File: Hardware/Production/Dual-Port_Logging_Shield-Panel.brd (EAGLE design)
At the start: 137.4 x 177.3 mm, 1686 parts, among them IC1 USB224X_2241_V04, IC10 USB224X_2241_V04, IC11 USB224X_2241_V04, IC12 USB224X_2241_V04, IC13 USB224X_2241_V04, IC14 USB224X_2241_V04, IC2 USB224X_2241_V04, IC3 USB224X_2241_V04, IC4 USB224X_2241_V04, IC5 USB224X_2241_V04, IC6 USB224X_2241_V04, IC7 USB224X_2241_V04, IC8 USB224X_2241_V04, IC9 USB224X_2241_V04, J10 MICRO-SD-PUSH-PUSH-EXT-PIN, J11 AVR_SPI_PROG_3X2TESTPOINTS, J12 THING_PLUS, J14 MICRO-SD-PUSH-PUSH-EXT-PIN, J15 AVR_SPI_PROG_3X2TESTPOINTS, J16 THING_PLUS, J18 MICRO-SD-PUSH-PUSH-EXT-PIN, J19 AVR_SPI_PROG_3X2TESTPOINTS, J2 MICRO-SD-PUSH-PUSH-EXT-PIN, J20 THING_PLUS, J22 MICRO-SD-PUSH-PUSH-EXT-PIN, J23 AVR_SPI_PROG_3X2TESTPOINTS, J24 THING_PLUS, J26 MICRO-SD-PUSH-PUSH-EXT-PIN, J27 AVR_SPI_PROG_3X2TESTPOINTS, J28 THING_PLUS, J3 AVR_SPI_PROG_3X2TESTPOINTS, J30 MICRO-SD-PUSH-PUSH-EXT-PIN, J31 AVR_SPI_PROG_3X2TESTPOINTS, J32 THING_PLUS, J34 MICRO-SD-PUSH-PUSH-EXT-PIN, J35 AVR_SPI_PROG_3X2TESTPOINTS, J36 THING_PLUS, J38 MICRO-SD-PUSH-PUSH-EXT-PIN, J39 AVR_SPI_PROG_3X2TESTPOINTS, J4 THING_PLUS, J40 THING_PLUS, J42 MICRO-SD-PUSH-PUSH-EXT-PIN, J43 AVR_SPI_PROG_3X2TESTPOINTS, J44 THING_PLUS, J46 MICRO-SD-PUSH-PUSH-EXT-PIN, J47 AVR_SPI_PROG_3X2TESTPOINTS, J48 THING_PLUS, J50 MICRO-SD-PUSH-PUSH-EXT-PIN, J51 AVR_SPI_PROG_3X2TESTPOINTS, J52 THING_PLUS, J54 MICRO-SD-PUSH-PUSH-EXT-PIN, J55 AVR_SPI_PROG_3X2TESTPOINTS, J56 THING_PLUS, J6 MICRO-SD-PUSH-PUSH-EXT-PIN, J7 AVR_SPI_PROG_3X2TESTPOINTS, J8 THING_PLUS, Q1 20V/4.2A/52mΩ/1.4W, Q10 20V/0.2A/8MHz/1.2Ω/1Vth, Q11 20V/4.2A/52mΩ/1.4W, Q13 20V/4.2A/52mΩ/1.4W, Q15 20V/4.2A/52mΩ/1.4W, Q16 20V/4.2A/52mΩ/1.4W, Q17 20V/0.2A/8MHz/1.2Ω/1Vth, Q18 20V/4.2A/52mΩ/1.4W, Q2 20V/0.2A/8MHz/1.2Ω/1Vth, Q20 20V/4.2A/52mΩ/1.4W, Q22 20V/4.2A/52mΩ/1.4W, Q23 20V/4.2A/52mΩ/1.4W, Q24 20V/0.2A/8MHz/1.2Ω/1Vth, Q25 20V/4.2A/52mΩ/1.4W, Q27 20V/4.2A/52mΩ/1.4W, Q29 20V/4.2A/52mΩ/1.4W, Q3 20V/4.2A/52mΩ/1.4W, Q30 20V/4.2A/52mΩ/1.4W, Q31 20V/0.2A/8MHz/1.2Ω/1Vth, Q32 20V/4.2A/52mΩ/1.4W, Q34 20V/4.2A/52mΩ/1.4W, Q36 20V/4.2A/52mΩ/1.4W, Q37 20V/4.2A/52mΩ/1.4W, Q38 20V/0.2A/8MHz/1.2Ω/1Vth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

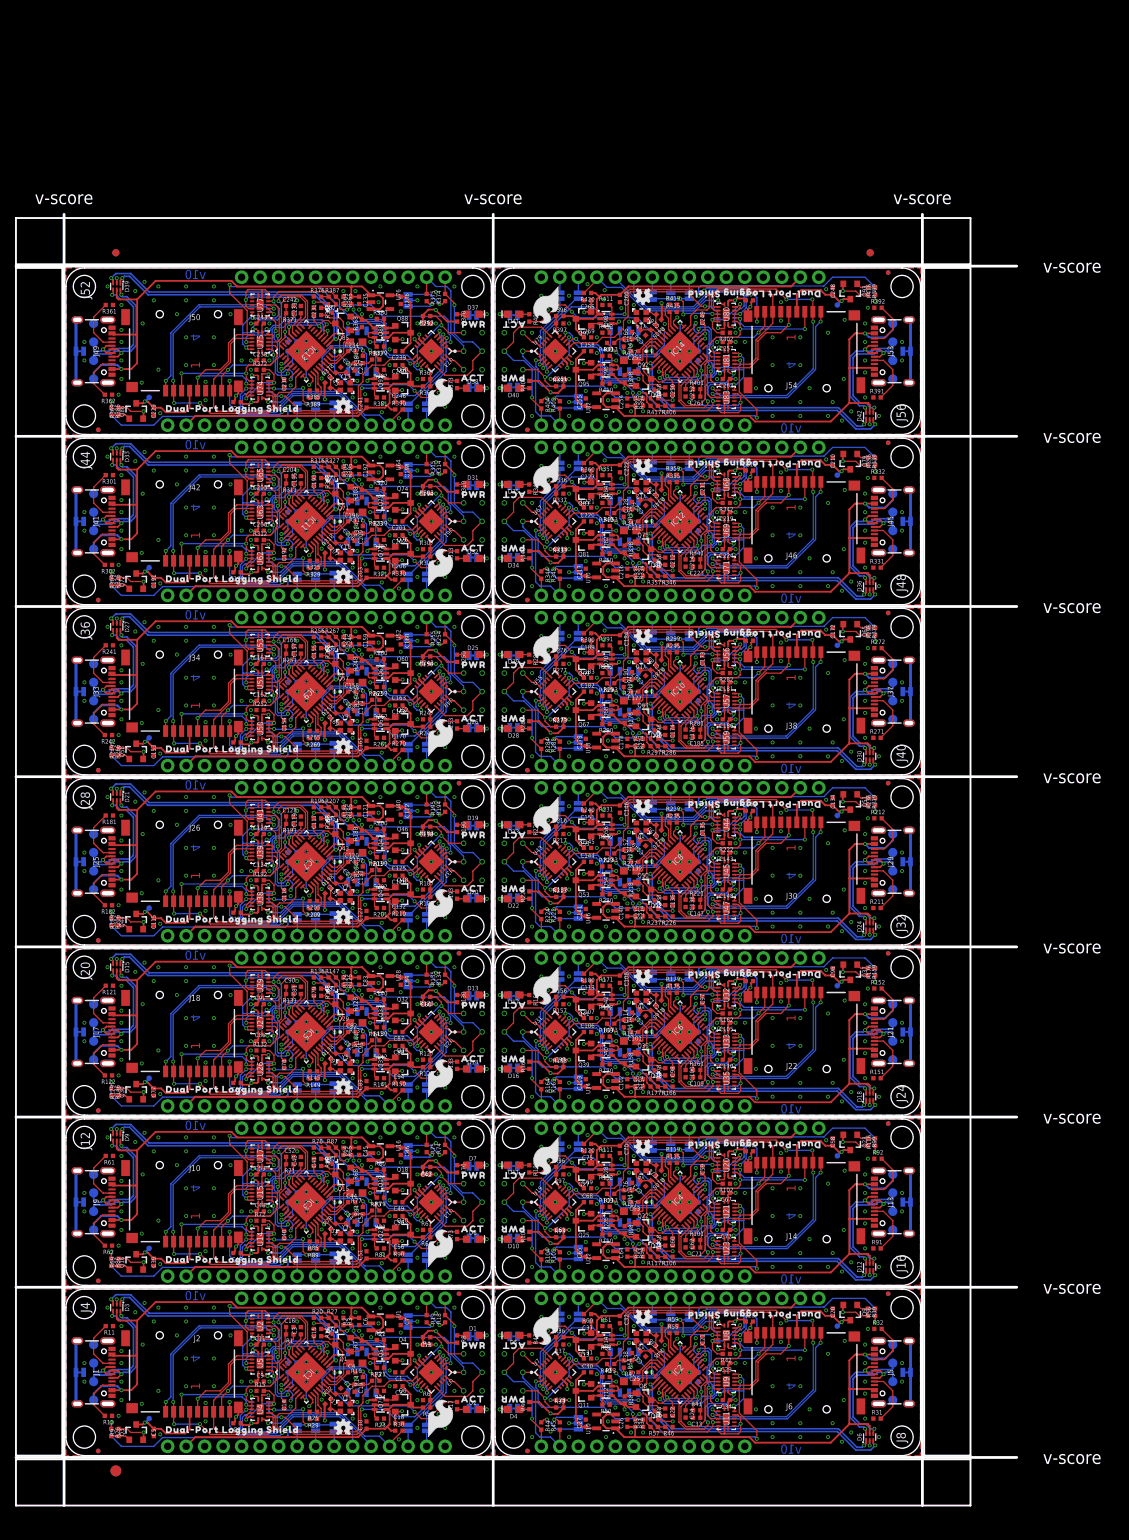
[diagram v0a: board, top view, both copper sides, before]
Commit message: Updated hardware files after REDS Review
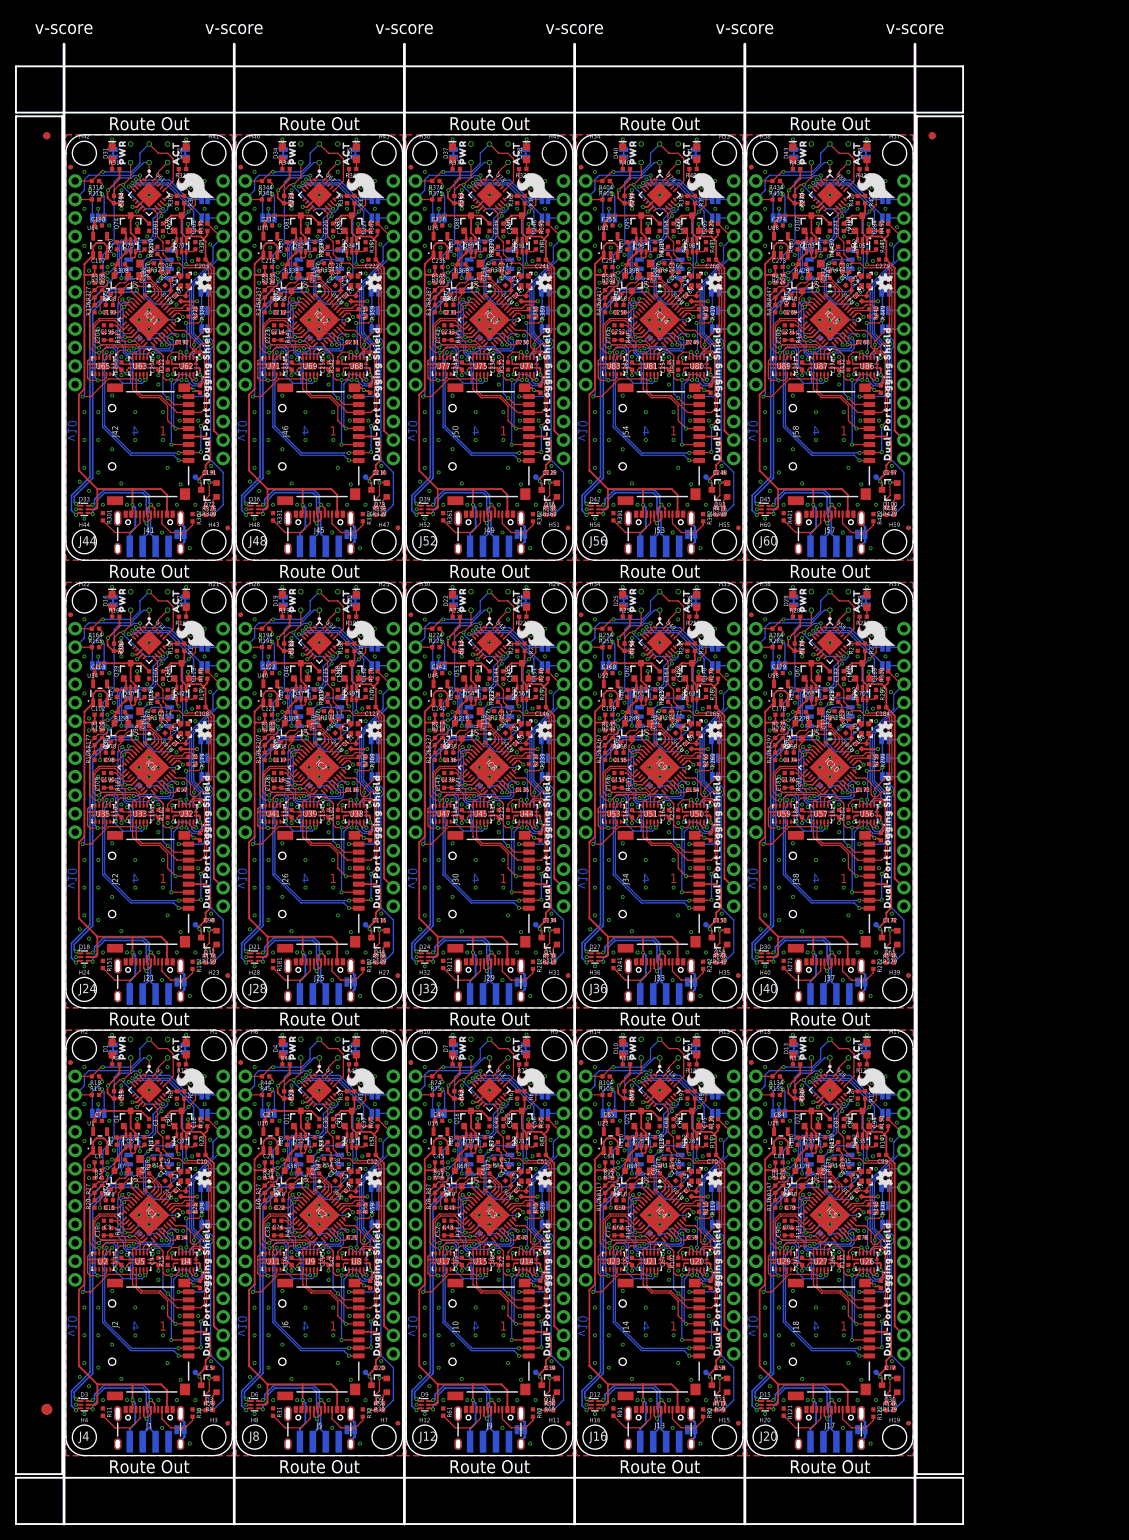
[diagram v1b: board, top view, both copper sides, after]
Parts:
- removed D+, D+1, D+10, D+11, D+12, D+13, D+2, D+3, D+4, D+5, D+6, D+7, D+8, D+9, D-, D-1, D-10, D-11, D-12, D-13, D-2, D-3, D-4, D-5, D-6, D-7, D-8, D-9, GND, GND1, GND10, GND11, GND12, GND13, GND2, GND3, GND4, GND5, GND6, GND7, GND8, GND9, V_USB, V_USB1, V_USB10, V_USB11, V_USB12, V_USB13, V_USB2, V_USB3, V_USB4, V_USB5, V_USB6, V_USB7, V_USB8, V_USB9: TEST-POINT3X5, SparkFun-Connectors:PAD.03X.05
- added C267, C268, C270, C275, C276, C277, C278, C280, C281, C285: 0.1uF, SparkFun-Capacitors:0402-TIGHT
- added C269, C271, C272, C273, C274, C279, C284: 2.2uF, SparkFun-Capacitors:0402-TIGHT
- added C282, C283: 12pF, SparkFun-Capacitors:0402-TIGHT
- added D43: RED, SparkFun-LED:LED-0603
- added D44: Yellow, SparkFun-LED:LED-0603
- added D45: PRTR5V0U2F, SparkFun-IC-Power:SOT886
- added FD57, FD58, FD59, FD60: FIDUCIALUFIDUCIAL, SparkFun-Aesthetics:FIDUCIAL-MICRO
- added GPIO15, MICROSD_VCC14, SDIO_!RESET!14, SDIO_VDD14: TEST-POINT3, SparkFun-Connectors:PAD.03X.03
- added H1, H10, H11, H12, H13, H14, H15, H16, H17, H18, H19, H2, H20, H21, H22, H23, H24, H25, H26, H27, H28, H29, H3, H30, H31, H32, H33, H34, H35, H36, H37, H38, H39, H4, H40, H41, H42, H43, H44, H45, H46, H47, H48, H49, H5, H50, H51, H52, H53, H54, H55, H56, H57, H58, H59, H6, H60, H7, H8, H9: STAND-OFF, SparkFun-Hardware:STAND-OFF
- added I2C14: JUMPER-SMT_3_NO_SILK, SparkFun-Jumpers:SMT-JUMPER_3_NO_SILK
- added IC15: USB224X_2241_V04, SparkFun-IC-Special-Function:36-QFN
- added J57: (no value), SparkFun-Connectors:USB-C-16P_4LAYER-PADS
- added J58: MICRO-SD-PUSH-PUSH-EXT-PIN, SparkFun-Connectors:MICROSD-EXTERNALPIN
- added J59: AVR_SPI_PROG_3X2TESTPOINTS, SparkFun-Connectors:2X3_TEST_POINTS
- added J60: THING_PLUS, SparkFun-Boards:THING_PLUS
- added JP43, JP46, JP47, JP50, JP51, JP54, JP55, JP58, JP59, RXD14, TXD14: JUMPER-SMT_2_NO_SILK, SparkFun-Jumpers:SMT-JUMPER_2_NO_SILK
- added JP44, JP48, JP52, JP56, JP60: USB_SOLDER_PADS, SparkFun-Connectors:USB-SOLDER-PADS
- added JP45, JP49, JP53, JP57, LED29, LED30: JUMPER-SMT_2_NC_TRACE_SILK, SparkFun-Jumpers:SMT-JUMPER_2_NC_TRACE_SILK
- added LOGO57, LOGO58: OSHW-LOGOMINI, SparkFun-Aesthetics:OSHW-LOGO-MINI
- added LOGO59: SFE_LOGO_FLAME.2_INCH, SparkFun-Aesthetics:SFE_LOGO_FLAME_.2
- added LOGO60: SFE_LOGO_NAME_FLAME.1_INCH, SparkFun-Aesthetics:SFE_LOGO_NAME_FLAME_.1
- added Q100, Q102, Q104, Q99: 20V/4.2A/52mΩ/1.4W, SparkFun-DiscreteSemi:SOT23-3
- added Q101: 20V/0.2A/8MHz/1.2Ω/1Vth, SparkFun-DiscreteSemi:SOT-416FL
- added Q103, Q105: (no value), SparkFun-DiscreteSemi:SOT363_PHILIPS
- added R421, R422: 5.1k, SparkFun-Resistors:0402-TIGHT
- added R423, R424, R425, R443, R444, R445, R449, R450: 10k, SparkFun-Resistors:0402-TIGHT
- added R426, R427, R428, R429, R431, R432, R436, R439, R441: 100k, SparkFun-Resistors:0402-TIGHT
- added R430, R433: 1k, SparkFun-Resistors:0402-TIGHT
- added R434, R435: 2.2k, SparkFun-Resistors:0402-TIGHT
- added R437: 12k, SparkFun-Resistors:0603
- added R438, R440, R442: 1M, SparkFun-Resistors:0402-TIGHT
- added R446, R447, R448: 100, SparkFun-Resistors:0402-TIGHT
- added SH14: JUMPER-SMT_2_NC_TRACE_NO-SILK, SparkFun-Jumpers:SMT-JUMPER_2_NC_TRACE_NO-SILK
- added U$337: (no value), output:PWR0
- added U$338: (no value), output:ACT0
- added U$339: (no value), output:#I�C#0
- added U$340: (no value), output:#PWR#0
- added U$341: (no value), output:#ACT#0
- added U$342, U$343: (no value), output:DUAL#PORT_LOGGING_SHIELD0
- added U$344: (no value), output:#SDA#0
- added U$345: (no value), output:#SCL#1
- added U$346: (no value), output:#RXD#0
- added U$347: (no value), output:#TXD#1
- added U$348: (no value), output:#POCI#0
- added U$349: (no value), output:#PICO#1
- added U$350: (no value), output:#SCK#2
- added U$351: (no value), output:#A5__#CS##0
- added U$352: (no value), output:#A4__#CS##6
- added U$353: (no value), output:#A3__#CS##6
- added U$354: (no value), output:#GND#0
- added U$355: (no value), output:#3V3#1
- added U$356: (no value), output:G0
- added U$357: (no value), output:V0
- added U$358: (no value), output:D#0
- added U$359: (no value), output:D#1
- added U$360: (no value), output:SH0
- added U85: ATTINY841-ARDUINO_QFN20M1, SparkFun-IC-Microcontroller:QFN20_20M1
- added U86, U87, U89: 74HC4066_QUAD_BILATERAL_SWITCH_QFN, SparkFun-IC-Logic:14-QFN
- added U88: 3.3V, SparkFun-IC-Power:SOT23-5
- added U90: 24C04, SparkFun-IC-Memory:SO08
- added Y15: 24MHz, SparkFun-Clocks:CRYSTAL-SMD-2.0X1.6MM
- J12, J16, J20, J24, J28, J32, J36, J4, J40, J44, J48, J52, J56, J8: device Thing_Plus:THING_PLUS -> SparkFun-Boards:THING_PLUS
- JP10, JP19, JP22, JP31, JP34, JP7: value JUMPER-SMT_2_NC_TRACE_SILK -> JUMPER-SMT_2_NO_SILK; device SparkFun-Jumpers:SMT-JUMPER_2_NC_TRACE_SILK -> SparkFun-Jumpers:SMT-JUMPER_2_NO_SILK
- JP12, JP20, JP24, JP32, JP36, JP8: value JUMPER-SMT_2_NO_SILK -> USB_SOLDER_PADS; device SparkFun-Jumpers:SMT-JUMPER_2_NO_SILK -> SparkFun-Connectors:USB-SOLDER-PADS
- JP16, JP28, JP4, JP40: value JUMPER-SMT_2_NC_TRACE_SILK -> USB_SOLDER_PADS; device SparkFun-Jumpers:SMT-JUMPER_2_NC_TRACE_SILK -> SparkFun-Connectors:USB-SOLDER-PADS
- JP17, JP21, JP29, JP33, JP41, JP5, JP9: value JUMPER-SMT_2_NO_SILK -> JUMPER-SMT_2_NC_TRACE_SILK; device SparkFun-Jumpers:SMT-JUMPER_2_NO_SILK -> SparkFun-Jumpers:SMT-JUMPER_2_NC_TRACE_SILK
- SH, SH1, SH10, SH11, SH12, SH13, SH2, SH3, SH4, SH5, SH6, SH7, SH8, SH9: value JUMPER-SMT_2_NC_TRACE_SILK -> JUMPER-SMT_2_NC_TRACE_NO-SILK; device SparkFun-Jumpers:SMT-JUMPER_2_NC_TRACE_SILK -> SparkFun-Jumpers:SMT-JUMPER_2_NC_TRACE_NO-SILK
- U$120, U$144, U$168, U$192, U$20, U$216, U$240, U$264, U$288, U$312, U$336, U$48, U$72, U$96: device output:#SH#0 -> output:SH0
- moved U$120 122.9 mm to (110.7, 3.56)
- moved SH4 120.4 mm to (109.2, 3.56), turned to 0 degrees
- moved U$116 119.4 mm to (107.6, 4.19)
- moved FD18 119.2 mm to (115.7, 4.45), turned to 0 degrees
- moved FD19 119.2 mm to (115.7, 4.45), turned to 0 degrees
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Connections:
- new net !CS!14: JP57.2, JP58.2, JP59.2, U86.4
- new net !RESET!14: J59.5, R423.1, U85.13
- new net 3.3V14: C278.1, C279.1, J60.27, Q104.3, Q105.1, R426.2, R450.1
- new net 3V3_DIV_15: R426.1, R427.2, U85.15
- new net ACTIVITY14: IC15.1, R433.2
- new net AT_POCI14: J59.1, U85.20
- new net D+14: D45.1, IC15.2
- new net D+_IN14: D45.6, J57.A6, J57.B6, JP60.D+
- new net D-14: D45.3, IC15.3
- new net D-_IN14: D45.4, J57.A7, J57.B7, JP60.D-
- new net GND14: C267.2, C268.2, C269.2, C270.2, C271.2, C272.2, C273.2, C274.2, C275.2, C276.2, C277.2, C278.2, C279.2, C280.2, C281.2, C282.1, C283.1, C284.2, C285.2, D45.2, IC15.28, IC15.EPAD, J57.GND, J57.GND2, J58.10, J58.11, J58.12, J58.13, J58.6, J59.6, J60.25, JP60.GND, LED29.1, LED30.1, Q101.2, R421.1, R422.1, R425.1, R427.1, R432.1, R436.1, R437.1, R439.1, R440.1, R441.1, R442.1, R445.2, R449.2, SH14.2, U85.8, U85.PAD, U86.7, U86.EPAD, U87.7, U87.EPAD, U88.2, U89.12, U89.6, U89.7, U89.EPAD, U90.1, U90.2, U90.3, U90.4, U90.7
- new net GPIO57: IC15.27, R443.2, U90.5
- new net GPIO58: IC15.29, R445.1
- new net GPIO59: IC15.31, R444.2, U90.6
- new net GPIO60: GPIO15.1, IC15.21
- new net MICROSD_CLK/SCK14: J58.5, U85.12, U86.10, U87.9
- new net MICROSD_CMD/SDI14: J58.3, U86.9, U87.3
- new net MICROSD_D0/SDO14: J58.7, U86.2, U87.10
- new net MICROSD_D29: J58.1, U89.3
- new net MICROSD_D3/!CS!14: J58.2, U86.3, U89.2
- new net MICROSD_D30: J58.8, U87.2
- new net MICROSD_PWR_EN14: R446.1, U85.5
- new net MICROSD_VCC14: C267.1, J58.4, MICROSD_VCC14.1, Q100.3
- new net N$365: J57.A5, R421.2
- new net N$366: J57.B5, R422.2
- new net N$367: J60.19, JP57.1
- new net N$368: J60.20, JP58.1
- new net N$369: J60.21, JP59.1
- new net N$370: D43.A, R430.1
- new net N$371: D43.C, LED29.2
- new net N$372: D44.A, R433.1
- new net N$373: D44.C, LED30.2
- new net N$374: I2C14.3, R435.2
- new net N$375: I2C14.1, R434.1
- new net N$376: C271.1, IC15.13
- new net N$377: C272.1, IC15.34
- new net N$378: Q99.1, R428.1, R448.2
- new net N$379: IC15.35, R437.2
- new net N$380: J60.14, RXD14.1
- new net N$381: J60.15, TXD14.1
- new net N$382: Q103.2, Q103.5, Q103.6, R439.2
- new net N$383: Q102.1, Q103.3, R440.2
- new net N$384: Q105.2, Q105.5, Q105.6, R441.2
- new net N$385: Q104.1, Q105.3, R442.2
- new net N$386: Q100.1, R429.1, R446.2
- new net N$387: Q101.1, R436.2, R447.1
- new net N$388: Q101.3, R448.1
- new net N$389: J57.SHLD1, J57.SHLD2, J57.SHLD3, J57.SHLD4, SH14.1
- new net N$390: IC15.30, R449.1
- new net PICO14: J60.17, U86.8
- new net POCI14: J60.16, R450.2, U86.1
- new net RXD14: RXD14.2, U85.3
- new net SCL14: J59.3, J60.2, R435.1, U85.1
- new net SCLK14: J60.18, U86.11
- new net SDA14: J59.4, J60.1, R434.2, U85.16
- new net SDIO_!RESET!14: C280.1, IC15.18, R431.2, SDIO_!RESET!14.1
- new net SDIO_EN14: R447.2, U85.2, U87.12, U87.13, U87.5, U87.6, U89.13, U89.5
- new net SDIO_VDD14: C268.1, C269.1, C285.1, IC15.14, IC15.22, IC15.36, IC15.6, Q99.3, R431.1, R443.1, R444.1, SDIO_VDD14.1, U90.8
- new net SD_!CD!14: IC15.26, J58.9
- new net SD_CLK14: IC15.9, U87.8
- new net SD_CMD14: IC15.11, U87.4
- new net SD_D56: IC15.5, U87.11
- new net SD_D57: IC15.4, U87.1
- new net SD_D58: IC15.25, U89.4
- new net SD_D59: IC15.23, U89.1
- new net SPI_EN14: R432.2, U85.11, U86.12, U86.13, U86.5, U86.6
- new net TXD14: TXD14.2, U85.4
- new net VCC14: C270.1, C275.1, C276.1, C281.1, C284.1, I2C14.2, J59.2, Q100.2, Q102.2, Q103.4, Q104.2, Q105.4, Q99.2, R423.2, R428.2, R429.2, R430.2, U85.9, U86.14, U87.14, U89.14
- new net VCC_15: C274.1, C277.1, Q102.3, Q103.1, U88.5
- new net V_USB14: C273.1, D45.5, J57.VBUS1, J57.VBUS2, JP60.VBUS, R424.2, U88.1, U88.3
- new net V_USB_DIV_15: R424.1, R425.2, U85.14
- new net XTAL29: C283.2, IC15.32, R438.1, Y15.1
- new net XTAL30: C282.2, IC15.33, R438.2, Y15.3
- net !CS!1: now also JP7.2; no longer JP4.2
- net !CS!10: now also JP41.2, JP42.2, JP43.2; no longer JP31.2, JP32.2, JP33.2
- net !CS!11: now also JP45.2, JP46.2, JP47.2; no longer JP34.2, JP35.2, JP36.2
- net !CS!12: now also JP49.2, JP50.2, JP51.2; no longer JP37.2, JP38.2, JP39.2
- net !CS!13: now also JP53.2, JP54.2, JP55.2; no longer JP40.2, JP41.2, JP42.2
- net !CS!2: now also JP10.2, JP11.2; no longer JP7.2, JP8.2
- net !CS!3: now also JP13.2, JP14.2, JP15.2; no longer JP10.2, JP11.2, JP12.2
- net !CS!4: now also JP17.2, JP18.2, JP19.2; no longer JP13.2, JP14.2, JP15.2
- net !CS!5: now also JP21.2, JP22.2, JP23.2; no longer JP16.2, JP17.2, JP18.2
- net !CS!6: now also JP25.2, JP26.2, JP27.2; no longer JP19.2, JP20.2, JP21.2
- net !CS!7: now also JP29.2, JP30.2, JP31.2; no longer JP22.2, JP23.2, JP24.2
- net !CS!8: now also JP33.2, JP34.2, JP35.2; no longer JP25.2, JP26.2, JP27.2
- net !CS!9: now also JP37.2, JP38.2, JP39.2; no longer JP28.2, JP29.2, JP30.2
- net D+_IN: now also JP4.D+; no longer D+.1
- net D+_IN1: now also JP8.D+; no longer D+1.1
- net D+_IN10: now also JP44.D+; no longer D+10.1
- net D+_IN11: now also JP48.D+; no longer D+11.1
- net D+_IN12: now also JP52.D+; no longer D+12.1
- net D+_IN13: now also JP56.D+; no longer D+13.1
- net D+_IN2: now also JP12.D+; no longer D+2.1
- net D+_IN3: now also JP16.D+; no longer D+3.1
- net D+_IN4: now also JP20.D+; no longer D+4.1
- net D+_IN5: now also JP24.D+; no longer D+5.1
- net D+_IN6: now also JP28.D+; no longer D+6.1
- net D+_IN7: now also JP32.D+; no longer D+7.1
- net D+_IN8: now also JP36.D+; no longer D+8.1
- net D+_IN9: now also JP40.D+; no longer D+9.1
- net D-_IN: now also JP4.D-; no longer D-.1
- net D-_IN1: now also JP8.D-; no longer D-1.1
- net D-_IN10: now also JP44.D-; no longer D-10.1
- net D-_IN11: now also JP48.D-; no longer D-11.1
- net D-_IN12: now also JP52.D-; no longer D-12.1
- net D-_IN13: now also JP56.D-; no longer D-13.1
- net D-_IN2: now also JP12.D-; no longer D-2.1
- net D-_IN3: now also JP16.D-; no longer D-3.1
- net D-_IN4: now also JP20.D-; no longer D-4.1
- net D-_IN5: now also JP24.D-; no longer D-5.1
- net D-_IN6: now also JP28.D-; no longer D-6.1
- net D-_IN7: now also JP32.D-; no longer D-7.1
- net D-_IN8: now also JP36.D-; no longer D-8.1
- net D-_IN9: now also JP40.D-; no longer D-9.1
- net GND: now also JP4.GND; no longer GND.1
- net GND1: now also JP8.GND; no longer GND1.1
- net GND10: now also JP44.GND; no longer GND10.1
- net GND11: now also JP48.GND; no longer GND11.1
- net GND12: now also JP52.GND; no longer GND12.1
- net GND13: now also JP56.GND; no longer GND13.1
- net GND2: now also JP12.GND; no longer GND2.1
- net GND3: now also JP16.GND; no longer GND3.1
- net GND4: now also JP20.GND; no longer GND4.1
- net GND5: now also JP24.GND; no longer GND5.1
- net GND6: now also JP28.GND; no longer GND6.1
- net GND7: now also JP32.GND; no longer GND7.1
- net GND8: now also JP36.GND; no longer GND8.1
- net GND9: now also JP40.GND; no longer GND9.1
- net N$107: now also JP17.1; no longer JP13.1
- net N$108: now also JP18.1; no longer JP14.1
- net N$109: now also JP19.1; no longer JP15.1
- net N$133: now also JP21.1; no longer JP16.1
- net N$134: now also JP22.1; no longer JP17.1
- net N$135: now also JP23.1; no longer JP18.1
- net N$159: now also JP25.1; no longer JP19.1
- net N$160: now also JP26.1; no longer JP20.1
- net N$161: now also JP27.1; no longer JP21.1
- net N$185: now also JP29.1; no longer JP22.1
- net N$186: now also JP30.1; no longer JP23.1
- net N$187: now also JP31.1; no longer JP24.1
- net N$211: now also JP33.1; no longer JP25.1
- net N$212: now also JP34.1; no longer JP26.1
- net N$213: now also JP35.1; no longer JP27.1
- net N$237: now also JP37.1; no longer JP28.1
- net N$238: now also JP38.1; no longer JP29.1
- net N$239: now also JP39.1; no longer JP30.1
- net N$263: now also JP41.1; no longer JP31.1
- net N$264: now also JP42.1; no longer JP32.1
- net N$265: now also JP43.1; no longer JP33.1
- net N$289: now also JP45.1; no longer JP34.1
- net N$29: now also JP5.1; no longer JP4.1
- net N$290: now also JP46.1; no longer JP35.1
- net N$291: now also JP47.1; no longer JP36.1
- net N$30: now also JP6.1; no longer JP5.1
- net N$31: now also JP7.1; no longer JP6.1
- net N$315: now also JP49.1; no longer JP37.1
- net N$316: now also JP50.1; no longer JP38.1
- net N$317: now also JP51.1; no longer JP39.1
- net N$341: now also JP53.1; no longer JP40.1
- net N$342: now also JP54.1; no longer JP41.1
- net N$343: now also JP55.1; no longer JP42.1
- net N$55: now also JP9.1; no longer JP7.1
- net N$56: now also JP10.1; no longer JP8.1
- net N$57: now also JP11.1; no longer JP9.1
- net N$81: now also JP13.1; no longer JP10.1
- net N$82: now also JP14.1; no longer JP11.1
- net N$83: now also JP15.1; no longer JP12.1
- net V_USB: now also JP4.VBUS; no longer V_USB.1
- net V_USB1: now also JP8.VBUS; no longer V_USB1.1
- net V_USB10: now also JP44.VBUS; no longer V_USB10.1
- net V_USB11: now also JP48.VBUS; no longer V_USB11.1
- net V_USB12: now also JP52.VBUS; no longer V_USB12.1
- net V_USB13: now also JP56.VBUS; no longer V_USB13.1
- net V_USB2: now also JP12.VBUS; no longer V_USB2.1
- net V_USB3: now also JP16.VBUS; no longer V_USB3.1
- net V_USB4: now also JP20.VBUS; no longer V_USB4.1
- net V_USB5: now also JP24.VBUS; no longer V_USB5.1
- net V_USB6: now also JP28.VBUS; no longer V_USB6.1
- net V_USB7: now also JP32.VBUS; no longer V_USB7.1
- net V_USB8: now also JP36.VBUS; no longer V_USB8.1
- net V_USB9: now also JP40.VBUS; no longer V_USB9.1
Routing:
- net V_USB14: track 0.00 -> 67.5 mm, vias 0 -> 1
- net MICROSD_CLK/SCK14: track 0.00 -> 62.5 mm, vias 0 -> 4
- net MICROSD_PWR_EN14: track 0.00 -> 62.1 mm, vias 0 -> 4
- net SDIO_EN14: track 0.00 -> 52.2 mm, vias 0 -> 6
- net GND14: track 0.00 -> 46.6 mm, vias 0 -> 77
- net MICROSD_D3/!CS!14: track 0.00 -> 43.1 mm, vias 0 -> 4
- net 3.3V14: track 0.00 -> 41.4 mm
- net D-14: track 0.00 -> 39.5 mm, vias 0 -> 2
- net SPI_EN14: track 0.00 -> 39.0 mm, vias 0 -> 3
- net SDIO_VDD14: track 0.00 -> 38.0 mm, vias 0 -> 5
- net D+14: track 0.00 -> 37.1 mm, vias 0 -> 2
- net VCC14: track 0.00 -> 31.1 mm, vias 0 -> 12
- net PICO14: track 0.00 -> 26.1 mm, vias 0 -> 1
- net MICROSD_D29: track 0.00 -> 25.0 mm, vias 0 -> 2
- net POCI14: track 0.00 -> 23.2 mm, vias 0 -> 1
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- added copper zone on layer 1, net GND14
- added copper zone on layer 16, net GND14
- added copper zone on layer 2, net GND14
- added copper zone on layer 15, net VCC14
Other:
- board size 137.4 x 177.3 mm -> 130 x 203.2 mm
- board text added: "Route Out"

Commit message: PCB v1.1
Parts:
- added C286, C287, C288, C308, C309, C310, C311, C312, C332, C333, C334, C335, C336, C356, C357, C358, C359, C360: 10uF, SparkFun-Capacitors:0402-TIGHT
- added C289, C290, C292, C297, C298, C299, C300, C302, C303, C307, C313, C314, C316, C321, C322, C323, C324, C326, C327, C331, C337, C338, C340, C345, C346, C347, C348, C350, C351, C355: 0.1uF, SparkFun-Capacitors:0402-TIGHT
- added C291, C293, C294, C295, C296, C301, C306, C315, C317, C318, C319, C320, C325, C330, C339, C341, C342, C343, C344, C349, C354: 2.2uF, SparkFun-Capacitors:0402-TIGHT
- added C304, C305, C328, C329, C352, C353: 12pF, SparkFun-Capacitors:0402-TIGHT
- C100, C108, C121, C122, C132, C139, C146, C155, C158, C159, C170, C177, C178, C179, C193, C196, C203, C217, C227, C231, C235, C241, C25, C250, C252, C254, C255, C26, C265, C273, C274, C279, C43, C60, C62, C63, C81, C82, C83, C84, C98: value 2.2uF -> 0.1uF
- C104, C109, C114, C123, C125, C126, C128, C133, C147, C152, C162, C171, C173, C175, C181, C186, C199, C200, C205, C210, C219, C221, C223, C224, C229, C243, C247, C248, C258, C267, C270, C277, C29, C30, C31, C42, C53, C61, C66, C77, C78, C80, C85, C90, C99: value 0.1uF -> 2.2uF
- C111, C130, C131, C169, C187, C206, C207, C225, C226, C244, C283, C35, C36, C73, C74: value 12pF -> 0.1uF
- C113, C136, C160, C184, C208, C233, C41, C64, C65, C89: value 2.2uF -> 12pF
- C116, C118, C142, C143, C144, C164, C166, C167, C190, C191, C192, C20, C21, C213, C23, C237, C238, C239, C240, C261, C262, C285, C47, C48, C68, C69, C71, C72, C95, C96: value 0.1uF -> 10uF
- C117, C119, C120, C140, C141, C165, C189, C212, C214, C215, C216, C22, C236, C24, C260, C284, C44, C45, C46, C70, C94: value 2.2uF -> 10uF
- C137, C161, C185, C209, C232, C256, C257, C280, C281, C40, C88: value 0.1uF -> 12pF
- C149, C150, C245, C282, C54, C55: value 12pF -> 2.2uF
- C168, C188, C263, C264, C92, C93: value 12pF -> 10uF
- I2C, I2C1, I2C10, I2C11, I2C12, I2C13, I2C14, I2C2, I2C3, I2C4, I2C5, I2C6, I2C7, I2C8, I2C9: value JUMPER-SMT_3_NO_SILK -> JUMPER-SMT_3_2-NC_TRACE_SILK; device SparkFun-Jumpers:SMT-JUMPER_3_NO_SILK -> SparkFun-Jumpers:SMT-JUMPER_3_2-NC_TRACE_SILK
- moved C217 127.0 mm to (112.6, 74.4)
- moved C97 124.6 mm to (112.6, 12.9)
- moved C106 124.3 mm to (106.2, 26.7), turned to 90 degrees
- moved C98 122.1 mm to (109.3, 30.5), turned to 0 degrees
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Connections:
- net 3.3V1: now also C36.1, C37.1; no longer C31.1, C32.1
- net 3.3V10: now also C252.1, C253.1; no longer C202.1, C203.1
- net 3.3V11: now also C276.1, C277.1; no longer C221.1, C222.1
- net 3.3V12: now also C300.1, C301.1; no longer C240.1, C241.1
- net 3.3V13: now also C324.1, C325.1; no longer C259.1, C260.1
- net 3.3V14: now also C348.1, C349.1; no longer C278.1, C279.1
- net 3.3V2: now also C60.1, C61.1; no longer C50.1, C51.1
- net 3.3V3: now also C84.1, C85.1; no longer C69.1, C70.1
- net 3.3V4: now also C108.1, C109.1; no longer C88.1, C89.1
- net 3.3V5: now also C132.1, C133.1; no longer C107.1, C108.1
- net 3.3V6: now also C156.1, C157.1; no longer C126.1, C127.1
- net 3.3V7: now also C180.1, C181.1; no longer C145.1, C146.1
- net 3.3V8: now also C204.1, C205.1; no longer C164.1, C165.1
- net 3.3V9: now also C228.1, C229.1; no longer C183.1, C184.1
- net GND: now also C20.2, C21.2, C22.2, C23.2, C24.2
- net GND1: now also C35.2, C36.2, C39.2, C40.1, C41.1, C42.2, C43.2, C44.2, C45.2, C46.2, C47.2, C48.2; no longer C20.2, C21.2, C22.2, C23.2, C24.2, C35.1, C36.1
- net GND10: now also C241.2, C242.2, C243.2, C244.2, C245.2, C246.2, C247.2, C248.2, C249.2, C250.2, C251.2, C252.2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; no longer C191.2, C192.2, C193.2, C194.2, C195.2, C196.2, C197.2, C198.2, C199.2, C200.2, C201.2, C202.2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
- net GND11: now also C265.2, C266.2, C267.2, C268.2, C269.2, C270.2, C271.2, C272.2, C273.2, C274.2, C275.2, C276.2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; no longer C210.2, C211.2, C212.2, C213.2, C214.2, C215.2, C216.2, C217.2, C218.2, C219.2, C220.2, C221.2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
- net GND12: now also C289.2, C290.2, C291.2, C292.2, C293.2, C294.2, C295.2, C296.2, C297.2, C298.2, C299.2, C300.2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; no longer C229.2, C230.2, C231.2, C232.2, C233.2, C234.2, C235.2, C236.2, C237.2, C238.2, C239.2, C240.2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
- net GND13: now also C313.2, C314.2, C315.2, C316.2, C317.2, C318.2, C319.2, C320.2, C321.2, C322.2, C323.2, C324.2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; no longer C248.2, C249.2, C250.2, C251.2, C252.2, C253.2, C254.2, C255.2, C256.2, C257.2, C258.2, C259.2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
- net GND14: now also C337.2, C338.2, C339.2, C340.2, C341.2, C342.2, C343.2, C344.2, C345.2, C346.2, C347.2, C348.2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; no longer C267.2, C268.2, C269.2, C270.2, C271.2, C272.2, C273.2, C274.2, C275.2, C276.2, C277.2, C278.2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
- net GND2: now also C54.2, C55.2, C58.2, C59.2, C60.2, C61.2, C62.2, C63.2, C64.1, C65.1, C66.2, C67.2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; no longer C39.2, C40.2, C41.2, C42.2, C43.2, C44.2, C45.2, C46.2, C47.2, C48.2, C54.1, C55.1
- net GND3: now also C73.2, C74.2, C77.2, C78.2, C79.2, C80.2, C81.2, C82.2, C83.2, C84.2, C85.2, C86.2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; no longer C58.2, C59.2, C60.2, C61.2, C62.2, C63.2, C64.2, C65.2, C66.2, C67.2, C68.2, C69.2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
- net GND4: now also C100.2, C101.2, C102.2, C103.2, C104.2, C105.2, C106.2, C107.2, C108.2, C109.2, C110.2, C111.2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; no longer C77.2, C78.2, C79.2, C80.2, C81.2, C82.2, C83.2, C84.2, C85.2, C86.2, C87.2, C88.2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
- net GND5: now also C121.2, C122.2, C123.2, C124.2, C125.2, C126.2, C127.2, C128.2, C129.2, C130.2, C131.2, C132.2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; no longer C100.2, C101.2, C102.2, C103.2, C104.2, C105.2, C106.2, C107.2, C108.2, C109.2, C110.2, C111.1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
- net GND6: now also C145.2, C146.2, C147.2, C148.2, C149.2, C150.2, C151.2, C152.2, C153.2, C154.2, C155.2, C156.2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; no longer C115.2, C116.2, C117.2, C118.2, C119.2, C120.2, C121.2, C122.2, C123.2, C124.2, C125.2, C126.2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
- net GND7: now also C169.2, C170.2, C171.2, C172.2, C173.2, C174.2, C175.2, C176.2, C177.2, C178.2, C179.2, C180.2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; no longer C134.2, C135.2, C136.2, C137.2, C138.2, C139.2, C140.2, C141.2, C142.2, C143.2, C144.2, C145.2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
- net GND8: now also C193.2, C194.2, C195.2, C196.2, C197.2, C198.2, C199.2, C200.2, C201.2, C202.2, C203.2, C204.2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; no longer C153.2, C154.2, C155.2, C156.2, C157.2, C158.2, C159.2, C160.2, C161.2, C162.2, C163.2, C164.2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
- net GND9: now also C217.2, C218.2, C219.2, C220.2, C221.2, C222.2, C223.2, C224.2, C225.2, C226.2, C227.2, C228.2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; no longer C172.2, C173.2, C174.2, C175.2, C176.2, C177.2, C178.2, C179.2, C180.2, C181.2, C182.2, C183.2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
- net MICROSD_VCC1: now also C25.1; no longer C20.1
- net MICROSD_VCC10: now also C241.1; no longer C191.1
- net MICROSD_VCC11: now also C265.1; no longer C210.1
- net MICROSD_VCC12: now also C289.1; no longer C229.1
- net MICROSD_VCC13: now also C313.1; no longer C248.1
- net MICROSD_VCC14: now also C337.1; no longer C267.1
- net MICROSD_VCC2: now also C49.1; no longer C39.1
- net MICROSD_VCC3: now also C73.1; no longer C58.1
- net MICROSD_VCC4: now also C97.1; no longer C77.1
- net MICROSD_VCC5: now also C121.1; no longer C96.1
- net MICROSD_VCC6: now also C145.1; no longer C115.1
- net MICROSD_VCC7: now also C169.1; no longer C134.1
- net MICROSD_VCC8: now also C193.1; no longer C153.1
- net MICROSD_VCC9: now also C217.1; no longer C172.1
- net N$116: now also C101.1; no longer C81.1
- net N$117: now also C102.1; no longer C82.1
- net N$142: now also C125.1; no longer C100.1
- net N$143: now also C126.1; no longer C101.1
- net N$168: now also C149.1; no longer C119.1
- net N$169: now also C150.1; no longer C120.1
- net N$194: now also C173.1; no longer C138.1
- net N$195: now also C174.1; no longer C139.1
- net N$220: now also C197.1; no longer C157.1
- net N$221: now also C198.1; no longer C158.1
- net N$246: now also C221.1; no longer C176.1
- net N$247: now also C222.1; no longer C177.1
- net N$272: now also C245.1; no longer C195.1
- net N$273: now also C246.1; no longer C196.1
- net N$298: now also C269.1; no longer C214.1
- net N$299: now also C270.1; no longer C215.1
- net N$324: now also C293.1; no longer C233.1
- net N$325: now also C294.1; no longer C234.1
- net N$350: now also C317.1; no longer C252.1
- net N$351: now also C318.1; no longer C253.1
- net N$376: now also C341.1; no longer C271.1
- net N$377: now also C342.1; no longer C272.1
- net N$38: now also C29.1; no longer C24.1
- net N$39: now also C30.1; no longer C25.1
- net N$64: now also C53.1; no longer C43.1
- net N$65: now also C54.1; no longer C44.1
- net N$90: now also C77.1; no longer C62.1
- net N$91: now also C78.1; no longer C63.1
- net SDIO_!RESET!1: now also C38.1; no longer C33.1
- net SDIO_!RESET!10: now also C254.1; no longer C204.1
- net SDIO_!RESET!11: now also C278.1; no longer C223.1
- net SDIO_!RESET!12: now also C302.1; no longer C242.1
- net SDIO_!RESET!13: now also C326.1; no longer C261.1
- net SDIO_!RESET!14: now also C350.1; no longer C280.1
- net SDIO_!RESET!2: now also C62.1; no longer C52.1
- net SDIO_!RESET!3: now also C86.1; no longer C71.1
- net SDIO_!RESET!4: now also C110.1; no longer C90.1
- net SDIO_!RESET!5: now also C134.1; no longer C109.1
- net SDIO_!RESET!6: now also C158.1; no longer C128.1
- net SDIO_!RESET!7: now also C182.1; no longer C147.1
- net SDIO_!RESET!8: now also C206.1; no longer C166.1
- net SDIO_!RESET!9: now also C230.1; no longer C185.1
- net SDIO_VDD1: now also C26.1, C27.1, C43.1; no longer C21.1, C22.1, C38.1
- net SDIO_VDD10: now also C242.1, C243.1, C259.1; no longer C192.1, C193.1, C209.1
- net SDIO_VDD11: now also C266.1, C267.1, C283.1; no longer C211.1, C212.1, C228.1
- net SDIO_VDD12: now also C290.1, C291.1, C307.1; no longer C230.1, C231.1, C247.1
- net SDIO_VDD13: now also C314.1, C315.1, C331.1; no longer C249.1, C250.1, C266.1
- net SDIO_VDD14: now also C338.1, C339.1, C355.1; no longer C268.1, C269.1, C285.1
- net SDIO_VDD2: now also C50.1, C51.1, C67.1; no longer C40.1, C41.1, C57.1
- net SDIO_VDD3: now also C74.1, C75.1, C91.1; no longer C59.1, C60.1, C76.1
- net SDIO_VDD4: now also C115.1, C98.1, C99.1; no longer C78.1, C79.1, C95.1
- net SDIO_VDD5: now also C122.1, C123.1, C139.1; no longer C114.1, C97.1, C98.1
- net SDIO_VDD6: now also C146.1, C147.1, C163.1; no longer C116.1, C117.1, C133.1
- net SDIO_VDD7: now also C170.1, C171.1, C187.1; no longer C135.1, C136.1, C152.1
- net SDIO_VDD8: now also C194.1, C195.1, C211.1; no longer C154.1, C155.1, C171.1
- net SDIO_VDD9: now also C218.1, C219.1, C235.1; no longer C173.1, C174.1, C190.1
- net VCC: now also C20.1, C21.1, C22.1, C23.1, C24.1
- net VCC1: now also C33.1, C39.1, C42.1, C44.1, C45.1, C46.1, C47.1, C48.1; no longer C23.1, C29.1, C37.1
- net VCC10: now also C244.1, C249.1, C250.1, C255.1, C258.1, C260.1, C261.1, C262.1, C263.1, C264.1; no longer C194.1, C199.1, C200.1, C205.1, C208.1
- net VCC11: now also C268.1, C273.1, C274.1, C279.1, C282.1, C284.1, C285.1, C286.1, C287.1, C288.1; no longer C213.1, C218.1, C219.1, C224.1, C227.1
- net VCC12: now also C292.1, C297.1, C298.1, C303.1, C306.1, C308.1, C309.1, C310.1, C311.1, C312.1; no longer C232.1, C237.1, C238.1, C243.1, C246.1
- net VCC13: now also C316.1, C321.1, C322.1, C327.1, C330.1, C332.1, C333.1, C334.1, C335.1, C336.1; no longer C251.1, C256.1, C257.1, C262.1, C265.1
- net VCC14: now also C340.1, C345.1, C346.1, C351.1, C354.1, C356.1, C357.1, C358.1, C359.1, C360.1; no longer C270.1, C275.1, C276.1, C281.1, C284.1
- net VCC2: now also C52.1, C57.1, C58.1, C63.1, C66.1, C68.1, C69.1, C70.1, C71.1, C72.1; no longer C42.1, C47.1, C48.1, C53.1, C56.1
- net VCC3: now also C76.1, C81.1, C82.1, C87.1, C90.1, C92.1, C93.1, C94.1, C95.1, C96.1; no longer C61.1, C66.1, C67.1, C72.1, C75.1
- net VCC4: now also C100.1, C105.1, C106.1, C111.1, C114.1, C116.1, C117.1, C118.1, C119.1, C120.1; no longer C80.1, C85.1, C86.1, C91.1, C94.1
- net VCC5: now also C124.1, C129.1, C130.1, C135.1, C138.1, C140.1, C141.1, C142.1, C143.1, C144.1; no longer C104.1, C105.1, C110.1, C113.1, C99.1
- net VCC6: now also C148.1, C153.1, C154.1, C159.1, C162.1, C164.1, C165.1, C166.1, C167.1, C168.1; no longer C118.1, C123.1, C124.1, C129.1, C132.1
- net VCC7: now also C172.1, C177.1, C178.1, C183.1, C186.1, C188.1, C189.1, C190.1, C191.1, C192.1; no longer C137.1, C142.1, C143.1, C148.1, C151.1
- net VCC8: now also C196.1, C201.1, C202.1, C207.1, C210.1, C212.1, C213.1, C214.1, C215.1, C216.1; no longer C156.1, C161.1, C162.1, C167.1, C170.1
- net VCC9: now also C220.1, C225.1, C226.1, C231.1, C234.1, C236.1, C237.1, C238.1, C239.1, C240.1; no longer C175.1, C180.1, C181.1, C186.1, C189.1
- net VCC_10: now also C224.1, C227.1; no longer C179.1, C182.1
- net VCC_11: now also C248.1, C251.1; no longer C198.1, C201.1
- net VCC_12: now also C272.1, C275.1; no longer C217.1, C220.1
- net VCC_13: now also C296.1, C299.1; no longer C236.1, C239.1
- net VCC_14: now also C320.1, C323.1; no longer C255.1, C258.1
- net VCC_15: now also C344.1, C347.1; no longer C274.1, C277.1
- net VCC_2: now also C32.1, C35.1; no longer C27.1, C30.1
- net VCC_3: now also C56.1, C59.1; no longer C46.1, C49.1
- net VCC_4: now also C80.1, C83.1; no longer C65.1, C68.1
- net VCC_5: now also C104.1, C107.1; no longer C84.1, C87.1
- net VCC_6: now also C128.1, C131.1; no longer C103.1, C106.1
- net VCC_7: now also C152.1, C155.1; no longer C122.1, C125.1
- net VCC_8: now also C176.1, C179.1; no longer C141.1, C144.1
- net VCC_9: now also C200.1, C203.1; no longer C160.1, C163.1
- net V_USB1: now also C31.1; no longer C26.1
- net V_USB10: now also C247.1; no longer C197.1
- net V_USB11: now also C271.1; no longer C216.1
- net V_USB12: now also C295.1; no longer C235.1
- net V_USB13: now also C319.1; no longer C254.1
- net V_USB14: now also C343.1; no longer C273.1
- net V_USB2: now also C55.1; no longer C45.1
- net V_USB3: now also C79.1; no longer C64.1
- net V_USB4: now also C103.1; no longer C83.1
- net V_USB5: now also C127.1; no longer C102.1
- net V_USB6: now also C151.1; no longer C121.1
- net V_USB7: now also C175.1; no longer C140.1
- net V_USB8: now also C199.1; no longer C159.1
- net V_USB9: now also C223.1; no longer C178.1
- net XTAL10: now also C112.2; no longer C92.2
- net XTAL11: now also C137.2; no longer C112.2
- net XTAL12: now also C136.2; no longer C111.2
- net XTAL13: now also C161.2; no longer C131.2
- net XTAL14: now also C160.2; no longer C130.2
- net XTAL15: now also C185.2; no longer C150.2
- net XTAL16: now also C184.2; no longer C149.2
- net XTAL17: now also C209.2; no longer C169.2
- net XTAL18: now also C208.2; no longer C168.2
- net XTAL19: now also C233.2; no longer C188.2
- net XTAL20: now also C232.2; no longer C187.2
- net XTAL21: now also C257.2; no longer C207.2
- net XTAL22: now also C256.2; no longer C206.2
- net XTAL23: now also C281.2; no longer C226.2
- net XTAL24: now also C280.2; no longer C225.2
- net XTAL25: now also C305.2; no longer C245.2
- net XTAL26: now also C304.2; no longer C244.2
- net XTAL27: now also C329.2; no longer C264.2
- net XTAL28: now also C328.2; no longer C263.2
- net XTAL29: now also C353.2; no longer C283.2
- net XTAL3: now also C41.2; no longer C36.2
- net XTAL30: now also C352.2; no longer C282.2
- net XTAL4: now also C40.2; no longer C35.2
- net XTAL5: now also C65.2; no longer C55.2
- net XTAL6: now also C64.2; no longer C54.2
- net XTAL7: now also C89.2; no longer C74.2
- net XTAL8: now also C88.2; no longer C73.2
- net XTAL9: now also C113.2; no longer C93.2
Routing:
- net VCC10: track 31.1 -> 40.6 mm, vias 12 -> 16
- net VCC14: track 31.1 -> 40.6 mm, vias 12 -> 16
- net VCC12: track 31.1 -> 40.6 mm, vias 12 -> 16
- net VCC11: track 31.1 -> 40.6 mm, vias 12 -> 16
- net VCC4: track 31.1 -> 40.6 mm, vias 12 -> 16
- net VCC: track 31.1 -> 40.6 mm, vias 12 -> 16
- net VCC13: track 31.1 -> 40.6 mm, vias 12 -> 16
- net VCC9: track 31.1 -> 40.6 mm, vias 12 -> 16
- net VCC2: track 31.1 -> 40.6 mm, vias 12 -> 16
- net VCC3: track 31.1 -> 40.6 mm, vias 12 -> 16
- net VCC7: track 31.1 -> 40.6 mm, vias 12 -> 16
- net VCC5: track 31.1 -> 40.6 mm, vias 12 -> 16
- net VCC1: track 31.1 -> 40.6 mm, vias 12 -> 16
- net VCC6: track 31.1 -> 40.6 mm, vias 12 -> 16
- net VCC8: track 31.1 -> 40.6 mm, vias 12 -> 16
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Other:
- board text added: "v11"
- board text removed: "v10"
